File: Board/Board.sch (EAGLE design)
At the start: 65 parts, among them IC1 MEGA8-AI, IC2 LM358D, IC4 MCP3426, IC6 MCP4921, IC7 TL431CD, Q1 IRLIZ44N, T1 BC817, U1 CJT1117-3.3-SOT223, U3 MCP9701AT-E/TT, U4 IRLML2502

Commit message: firmware improvements
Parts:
- IC1: value MEGA8-AI -> MEGA328
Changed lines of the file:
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@@
 <part name="+3V7" library="supply1" library_urn="urn:adsk.eagle:library:371" deviceset="+3V3" device=""/>
 <part name="U1" library="Seeed-OPL-ic" deviceset="PMIC-CJT1117-3.3(SOT223)" device="" value="CJT1117-3.3-SOT223"/>
-<part name="IC1" library="atmel" library_urn="urn:adsk.eagle:library:105" deviceset="MEGA8" device="-AI" package3d_urn="urn:adsk.eagle:package:4313/1"/>
+<part name="IC1" library="atmel" library_urn="urn:adsk.eagle:library:105" deviceset="MEGA8" device="-AI" package3d_urn="urn:adsk.eagle:package:4313/1" value="MEGA328"/>
 <part name="U3" library="components" deviceset="MCP9701AT-E/TT" device=""/>
 <part name="+3V1" library="supply1" library_urn="urn:adsk.eagle:library:371" deviceset="+3V3" device=""/>

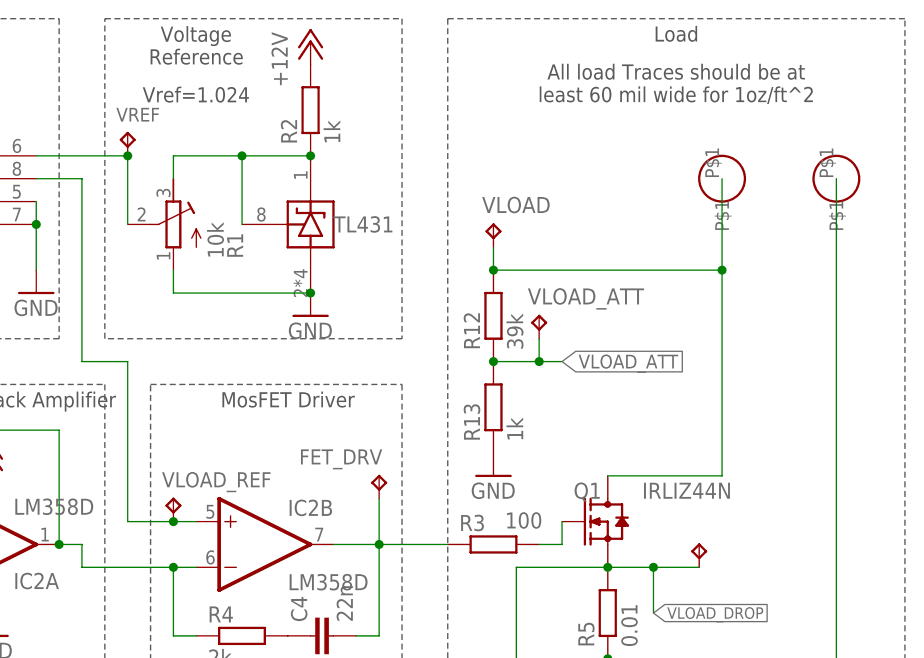
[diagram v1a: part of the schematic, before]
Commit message: added OSHW logo
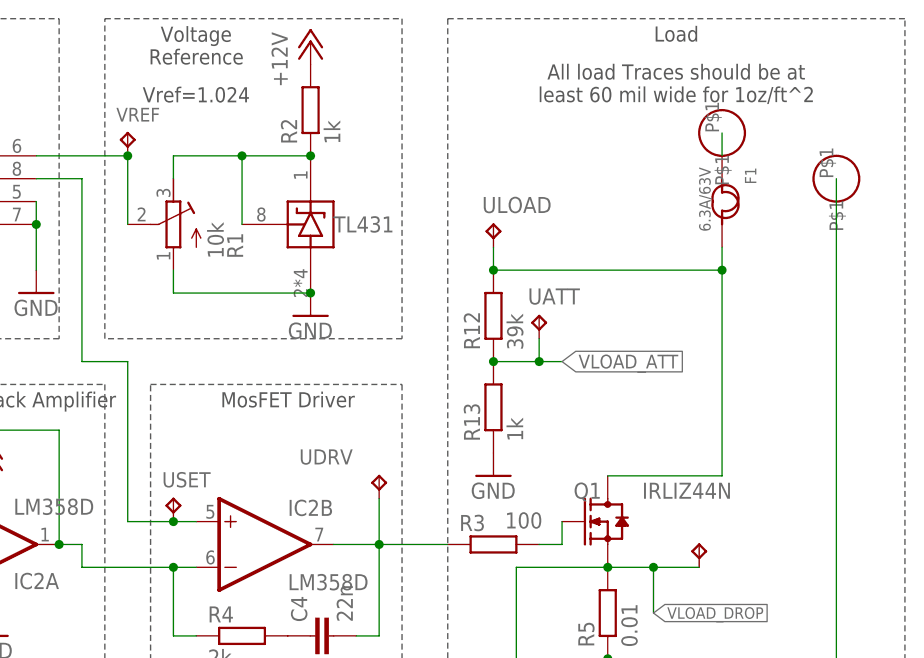
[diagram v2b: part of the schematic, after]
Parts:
- added F1: 6.3A/63V, Seeed-OPL-fuse:FUSE'1206'
- renumbered FET_DRV to UDRV, VLOAD to ULOAD, VLOAD_ATT to UATT, VLOAD_DROP to UDROP, VLOAD_REF to USET
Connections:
- new net N$7: F1.1, IN+.P$1
- net LOAD+: now also F1.2; no longer IN+.P$1
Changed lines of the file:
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@@
 <part name="R6" library="rcl" library_urn="urn:adsk.eagle:library:334" deviceset="R-EU_" device="R0603" package3d_urn="urn:adsk.eagle:package:23555/2" value="100"/>
 <part name="VREF" library="testpad" deviceset="TP" device="B1,27"/>
-<part name="VLOAD_REF" library="testpad" deviceset="TP" device="B1,27"/>
-<part name="FET_DRV" library="testpad" deviceset="TP" device="B1,27"/>
-<part name="VLOAD_DROP" library="testpad" deviceset="TP" device="B1,27"/>
-<part name="VLOAD" library="testpad" deviceset="TP" device="B1,27"/>
+<part name="USET" library="testpad" deviceset="TP" device="B1,27"/>
+<part name="UDRV" library="testpad" deviceset="TP" device="B1,27"/>
+<part name="UDROP" library="testpad" deviceset="TP" device="B1,27"/>
+<part name="ULOAD" library="testpad" deviceset="TP" device="B1,27"/>
 <part name="+3V3" library="testpad" deviceset="TP" device="B1,27"/>
 <part name="+12V" library="testpad" deviceset="TP" device="B1,27"/>
@@
 <part name="R12" library="rcl" deviceset="R-EU_" device="R0603" value="39k"/>
 <part name="R13" library="rcl" deviceset="R-EU_" device="R0603" value="1k"/>
-<part name="VLOAD_ATT" library="testpad" deviceset="TP" device="B1,27"/>
+<part name="UATT" library="testpad" deviceset="TP" device="B1,27"/>
 <part name="GND22" library="supply1" deviceset="GND" device=""/>
 <part name="FAN1" library="testpad" deviceset="TP" device="B1,27"/>
@@
 <part name="GND14" library="supply1" deviceset="GND" device=""/>
 <part name="GND15" library="supply1" deviceset="GND" device=""/>
+<part name="F1" library="Seeed-OPL-fuse" deviceset="FUSE" device="'1206'" value="6.3A/63V"/>
 </parts>
 <sheets>
@@
 <attribute name="TP_SIGNAL_NAME" x="232.41" y="85.09" size="1.778" layer="97"/>
 </instance>
-<instance part="VLOAD_REF" gate="G$1" x="236.22" y="45.72" smashed="yes">
+<instance part="USET" gate="G$1" x="236.22" y="45.72" smashed="yes">
 <attribute name="NAME" x="234.95" y="46.99" size="1.6764" layer="95"/>
 <attribute name="TP_SIGNAL_NAME" x="237.49" y="44.45" size="1.778" layer="97"/>
 </instance>
-<instance part="FET_DRV" gate="G$1" x="259.08" y="48.26" smashed="yes">
+<instance part="UDRV" gate="G$1" x="259.08" y="48.26" smashed="yes">
 <attribute name="NAME" x="250.19" y="49.53" size="1.6764" layer="95"/>
 <attribute name="TP_SIGNAL_NAME" x="260.35" y="46.99" size="1.778" layer="97"/>
 </instance>
-<instance part="VLOAD_DROP" gate="G$1" x="294.64" y="40.64" smashed="yes">
+<instance part="UDROP" gate="G$1" x="294.64" y="40.64" smashed="yes">
 <attribute name="TP_SIGNAL_NAME" x="295.91" y="39.37" size="1.778" layer="97"/>
 </instance>
-<instance part="VLOAD" gate="G$1" x="271.78" y="76.2"/>
+<instance part="ULOAD" gate="G$1" x="271.78" y="76.2"/>
 <instance part="+3V3" gate="G$1" x="154.94" y="86.36" smashed="yes">
 <attribute name="NAME" x="153.67" y="87.63" size="1.524" layer="95"/>
@@
 <instance part="R12" gate="G$1" x="271.78" y="66.04" rot="R90"/>
 <instance part="R13" gate="G$1" x="271.78" y="55.88" rot="R90"/>
-<instance part="VLOAD_ATT" gate="G$1" x="276.86" y="66.04"/>
+<instance part="UATT" gate="G$1" x="276.86" y="66.04"/>
 <instance part="GND22" gate="1" x="30.48" y="-15.24" rot="R270"/>
 <instance part="FAN1" gate="G$1" x="134.62" y="50.8" smashed="yes" rot="R90">
@@
 <instance part="R7" gate="G$1" x="200.66" y="35.56" rot="R90"/>
 <instance part="R8" gate="G$1" x="200.66" y="48.26" rot="R270"/>
-<instance part="IN+" gate="G$1" x="297.18" y="81.28"/>
+<instance part="IN+" gate="G$1" x="297.18" y="86.36"/>
 <instance part="IN-" gate="G$1" x="309.88" y="81.28"/>
 <instance part="S1" gate="G$1" x="81.28" y="-17.78" rot="R90"/>
@@
 <instance part="GND14" gate="1" x="83.82" y="33.02" rot="R270"/>
 <instance part="GND15" gate="1" x="83.82" y="40.64" rot="R270"/>
+<instance part="F1" gate="F" x="297.18" y="78.74" rot="R270"/>
 </instances>
 <busses>
@@
 <wire x1="226.06" y1="60.96" x2="231.14" y2="60.96" width="0.1524" layer="91"/>
 <wire x1="231.14" y1="60.96" x2="231.14" y2="43.18" width="0.1524" layer="91"/>
-<pinref part="VLOAD_REF" gate="G$1" pin="TP"/>
+<pinref part="USET" gate="G$1" pin="TP"/>
 <pinref part="IC2" gate="B" pin="+IN"/>
 <wire x1="236.22" y1="43.18" x2="231.14" y2="43.18" width="0.1524" layer="91"/>
@@
 <wire x1="284.48" y1="48.26" x2="297.18" y2="48.26" width="0.1524" layer="91"/>
 <wire x1="297.18" y1="48.26" x2="297.18" y2="71.12" width="0.1524" layer="91"/>
-<pinref part="VLOAD" gate="G$1" pin="TP"/>
-<wire x1="297.18" y1="71.12" x2="297.18" y2="81.28" width="0.1524" layer="91"/>
+<pinref part="ULOAD" gate="G$1" pin="TP"/>
+<wire x1="297.18" y1="71.12" x2="297.18" y2="73.66" width="0.1524" layer="91"/>
 <wire x1="271.78" y1="71.12" x2="271.78" y2="73.66" width="0.1524" layer="91"/>
 <junction x="297.18" y="71.12"/>
@@
 <wire x1="271.78" y1="71.12" x2="297.18" y2="71.12" width="0.1524" layer="91"/>
 <junction x="271.78" y="71.12"/>
-<pinref part="IN+" gate="G$1" pin="P$1"/>
+<pinref part="F1" gate="F" pin="2"/>
 </segment>
 </net>
@@
 <wire x1="274.32" y1="22.86" x2="274.32" y2="38.1" width="0.1524" layer="91"/>
 <wire x1="274.32" y1="38.1" x2="284.48" y2="38.1" width="0.1524" layer="91"/>
-<pinref part="VLOAD_DROP" gate="G$1" pin="TP"/>
+<pinref part="UDROP" gate="G$1" pin="TP"/>
 <label x="289.56" y="33.02" size="1.27" layer="95" xref="yes"/>
 <wire x1="289.56" y1="38.1" x2="289.56" y2="33.02" width="0.1524" layer="91"/>
@@
 <wire x1="259.08" y1="30.48" x2="259.08" y2="40.64" width="0.1524" layer="91"/>
 <junction x="259.08" y="40.64"/>
-<pinref part="FET_DRV" gate="G$1" pin="TP"/>
+<pinref part="UDRV" gate="G$1" pin="TP"/>
 <wire x1="259.08" y1="40.64" x2="259.08" y2="45.72" width="0.1524" layer="91"/>
 </segment>
@@
 <junction x="271.78" y="60.96"/>
 <label x="279.4" y="60.96" size="1.524" layer="95" xref="yes"/>
-<pinref part="VLOAD_ATT" gate="G$1" pin="TP"/>
+<pinref part="UATT" gate="G$1" pin="TP"/>
 <wire x1="276.86" y1="60.96" x2="279.4" y2="60.96" width="0.1524" layer="91"/>
 <wire x1="276.86" y1="63.5" x2="276.86" y2="60.96" width="0.1524" layer="91"/>
@@
 </segment>
 </net>
+<net name="N$7" class="0">
+<segment>
+<pinref part="IN+" gate="G$1" pin="P$1"/>
+<pinref part="F1" gate="F" pin="1"/>
+<wire x1="297.18" y1="83.82" x2="297.18" y2="86.36" width="0.1524" layer="91"/>
+</segment>
+</net>

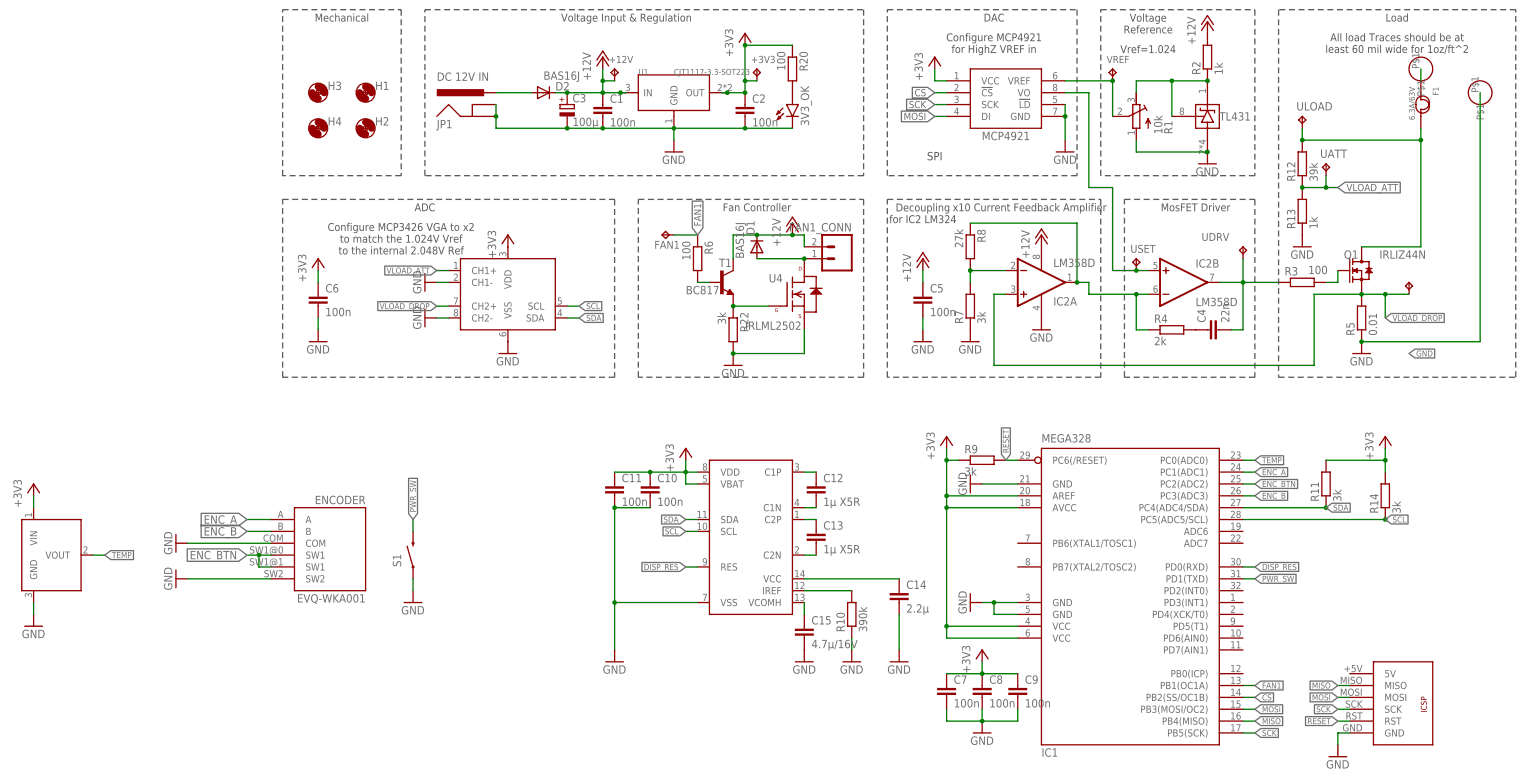
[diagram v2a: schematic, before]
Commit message: added zener to vload_att net to protect from overvoltage conditions
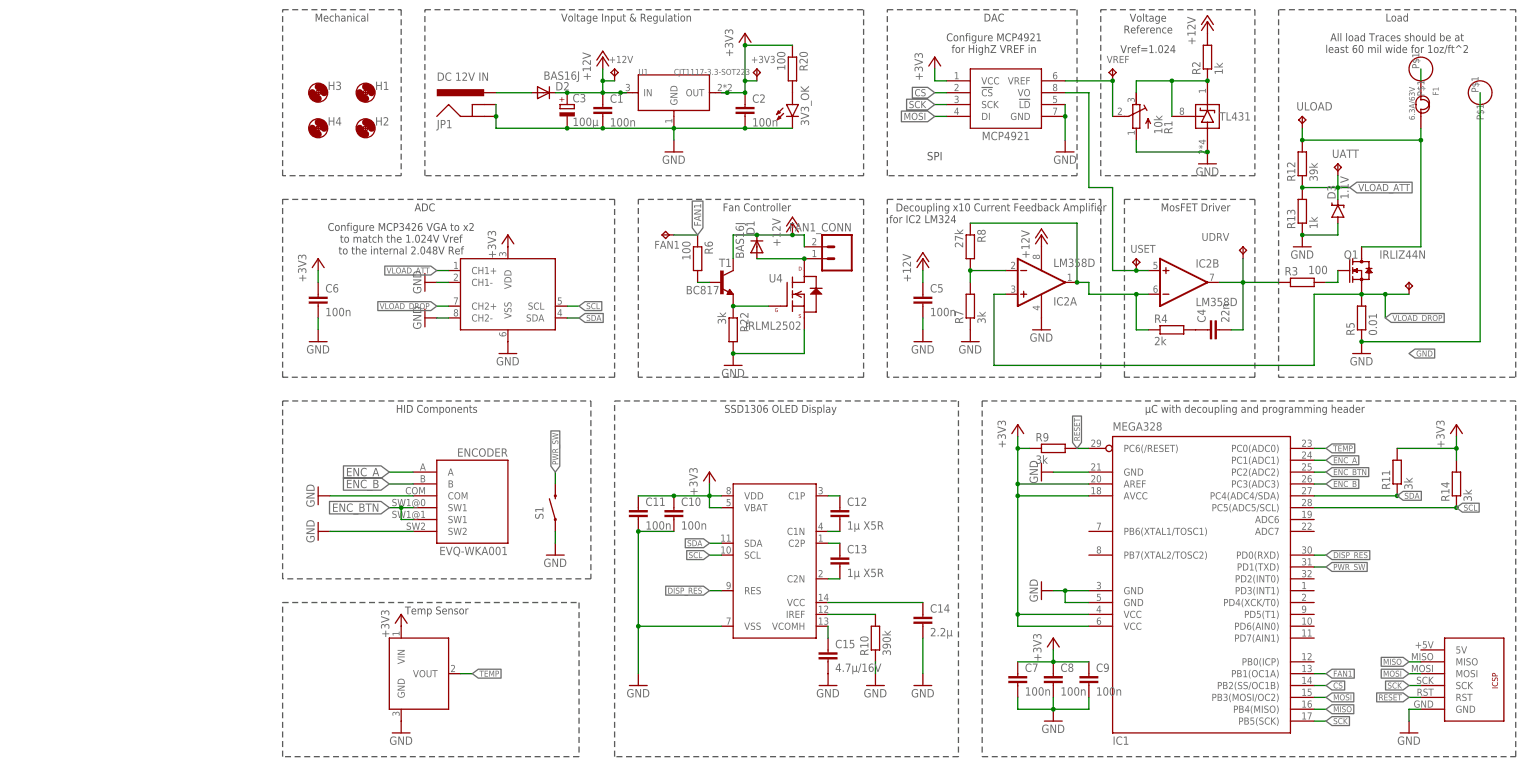
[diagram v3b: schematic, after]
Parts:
- added D3: 1.1V, SparkFun-DiscreteSemi:DIODE-ZENER5.6V
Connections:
- net GND: now also D3.A
- net VLOAD_ATT: now also D3.C
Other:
- note added: "HID Components"
- note added: "SSD1306 OLED Display"
- note added: "Temp Sensor"
- note added: "µC with decoupling and programming header"
- moved on the sheet: C10, C11, C12, C13, C14, C15, C7, C8, C9, ENCODER, IC1, R10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

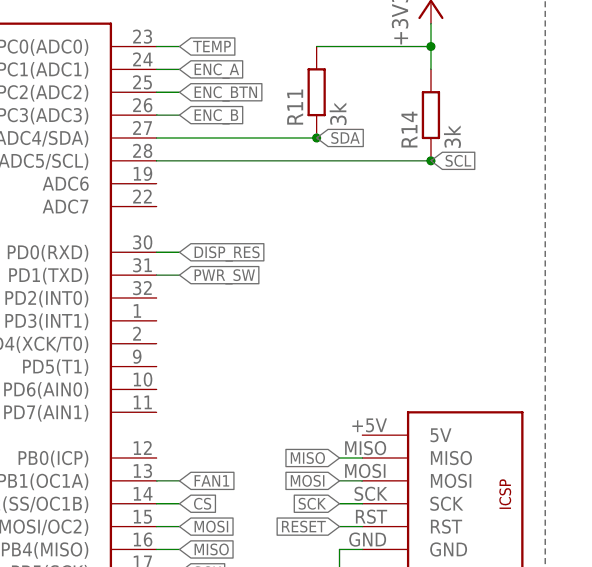
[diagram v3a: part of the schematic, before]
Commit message: added throughhole ICSP header
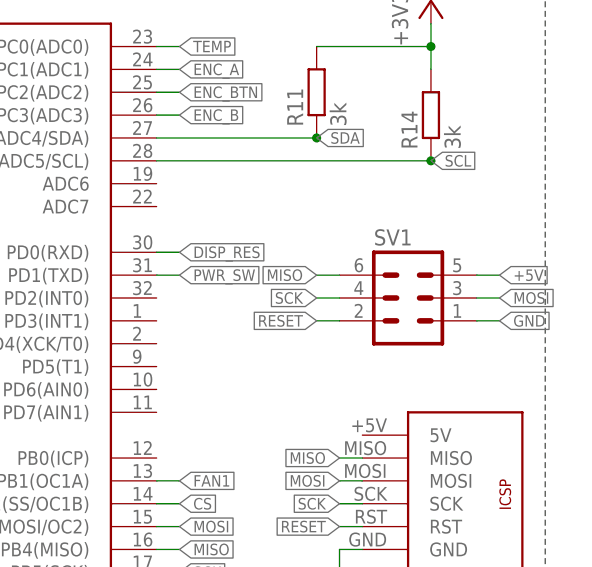
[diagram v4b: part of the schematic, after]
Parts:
- added SV1: (no value), con-lstb:MA03-2
- U$4: value ICSPSMD -> ICSP; device OwnStuff:ICSPSMD -> OwnStuff:ICSP
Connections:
- new net +5V: SV1.5
- net GND: now also SV1.1
- net MISO: now also SV1.6
- net MOSI: now also SV1.3
- net RESET: now also SV1.2
- net SCK: now also SV1.4
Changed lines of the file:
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@@
 <?xml version="1.0" encoding="utf-8"?>
 <!DOCTYPE eagle SYSTEM "eagle.dtd">
-<eagle version="8.3.1">
+<eagle version="8.4.0">
 <drawing>
 <settings>
@@
 <part name="+3V9" library="supply1" library_urn="urn:adsk.eagle:library:371" deviceset="+3V3" device=""/>
 <part name="GND24" library="supply1" deviceset="GND" device=""/>
-<part name="U$4" library="OwnStuff" deviceset="ICSP" device="SMD"/>
+<part name="U$4" library="OwnStuff" deviceset="ICSP" device="" value="ICSP"/>
 <part name="GND25" library="supply1" deviceset="GND" device=""/>
 <part name="R11" library="rcl" library_urn="urn:adsk.eagle:library:334" deviceset="R-EU_" device="R0603" package3d_urn="urn:adsk.eagle:package:23555/2" value="3k"/>
@@
 <part name="F1" library="Seeed-OPL-fuse" deviceset="FUSE" device="'1206'" value="6.3A/63V"/>
 <part name="D3" library="SparkFun-DiscreteSemi" deviceset="DIODE-ZENER" device="5.6V" value="1.1V"/>
+<part name="SV1" library="con-lstb" library_urn="urn:adsk.eagle:library:162" deviceset="MA03-2" device="" package3d_urn="urn:adsk.eagle:package:8334/1"/>
 </parts>
 <sheets>
@@
 <instance part="F1" gate="F" x="297.18" y="78.74" rot="R270"/>
 <instance part="D3" gate="G$1" x="279.4" y="55.88" rot="R90"/>
+<instance part="SV1" gate="1" x="302.26" y="-22.86"/>
 </instances>
 <busses>
@@
 <pinref part="GND15" gate="1" pin="GND"/>
 </segment>
+<segment>
+<pinref part="SV1" gate="1" pin="1"/>
+<wire x1="309.88" y1="-25.4" x2="312.42" y2="-25.4" width="0.1524" layer="91"/>
+<label x="312.42" y="-25.4" size="1.27" layer="95" xref="yes"/>
+</segment>
 </net>
 <net name="N$1" class="0">
@@
 <label x="294.64" y="-45.72" size="1.27" layer="95" rot="R180" xref="yes"/>
 </segment>
+<segment>
+<pinref part="SV1" gate="1" pin="4"/>
+<wire x1="294.64" y1="-22.86" x2="292.1" y2="-22.86" width="0.1524" layer="91"/>
+<label x="292.1" y="-22.86" size="1.27" layer="95" rot="R180" xref="yes"/>
+</segment>
 </net>
 <net name="MOSI" class="0">
@@
 <wire x1="297.18" y1="-43.18" x2="294.64" y2="-43.18" width="0.1524" layer="91"/>
 <label x="294.64" y="-43.18" size="1.27" layer="95" rot="R180" xref="yes"/>
+</segment>
+<segment>
+<pinref part="SV1" gate="1" pin="3"/>
+<wire x1="309.88" y1="-22.86" x2="312.42" y2="-22.86" width="0.1524" layer="91"/>
+<label x="312.42" y="-22.86" size="1.27" layer="95" xref="yes"/>
 </segment>
 </net>
@@
 <label x="294.64" y="-48.26" size="1.27" layer="95" rot="R180" xref="yes"/>
 </segment>
+<segment>
+<pinref part="SV1" gate="1" pin="2"/>
+<wire x1="294.64" y1="-25.4" x2="292.1" y2="-25.4" width="0.1524" layer="91"/>
+<label x="292.1" y="-25.4" size="1.27" layer="95" rot="R180" xref="yes"/>
+</segment>
 </net>
 <net name="MISO" class="0">
@@
 <label x="294.64" y="-40.64" size="1.27" layer="95" rot="R180" xref="yes"/>
 </segment>
+<segment>
+<pinref part="SV1" gate="1" pin="6"/>
+<wire x1="294.64" y1="-20.32" x2="292.1" y2="-20.32" width="0.1524" layer="91"/>
+<label x="292.1" y="-20.32" size="1.27" layer="95" rot="R180" xref="yes"/>
+</segment>
 </net>
 <net name="CS" class="0">
@@
 </segment>
 </net>
+<net name="+5V" class="0">
+<segment>
+<pinref part="SV1" gate="1" pin="5"/>
+<wire x1="309.88" y1="-20.32" x2="312.42" y2="-20.32" width="0.1524" layer="91"/>
+<label x="312.42" y="-20.32" size="1.27" layer="95" xref="yes"/>
+</segment>
+</net>
